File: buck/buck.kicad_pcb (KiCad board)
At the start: 2 copper layers, 37.8 x 17.8 mm, 15 parts, among them IC1 TPS630702RNMR

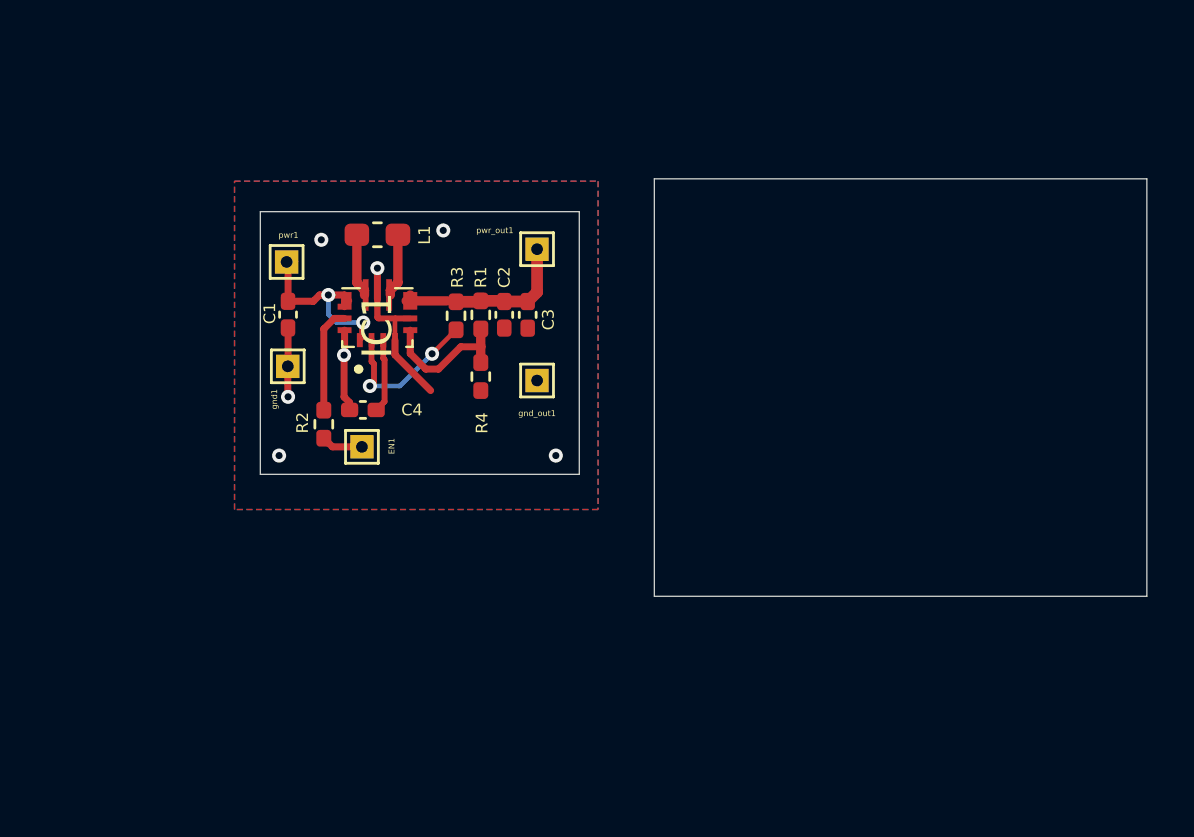
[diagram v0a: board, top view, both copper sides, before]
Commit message: removed esp32 comp
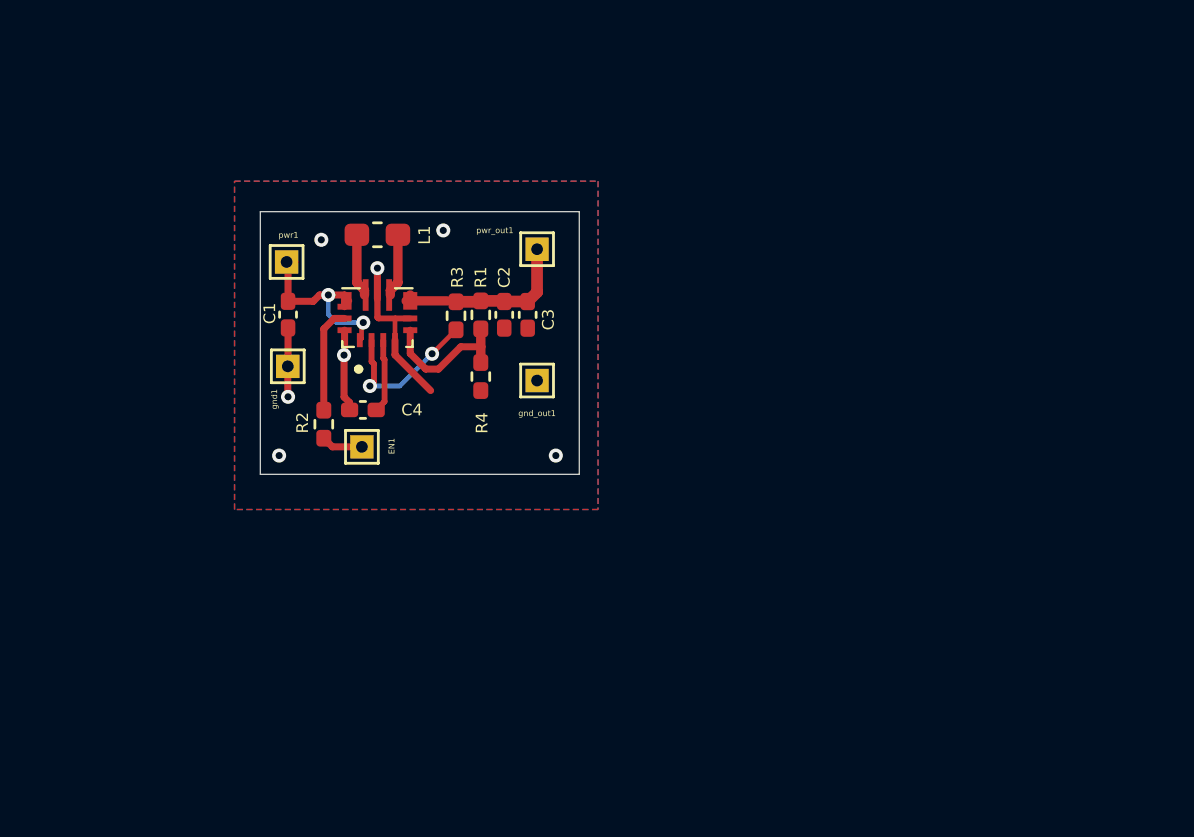
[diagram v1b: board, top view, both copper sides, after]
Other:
- board size 37.8 x 17.8 mm -> 13.6 x 11.2 mm
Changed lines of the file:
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@@
 			(at 0.194 0 90)
 			(layer "F.SilkS")
+			(hide yes)
 			(effects
 				(font
@@
 			)
 			(layer "F.Fab")
-		)
-		(fp_text user "${REFERENCE}"
-			(at 0.194 0 90)
-			(layer "F.Fab")
-			(effects
-				(font
-					(size 1.27 1.27)
-					(thickness 0.254)
-				)
-			)
 		)
 		(pad "1" smd rect
@@
 	)
 	(gr_rect
-		(start 176.4 63.4)
-		(end 197.4 81.2)
-		(stroke
-			(width 0.05)
-			(type default)
-		)
-		(fill no)
-		(layer "Edge.Cuts")
-	)
-	(gr_rect

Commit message: made prod, gave components for everything
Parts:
- C1, C3: footprint Capacitor_SMD:C_0402_1005Metric_Pad0.74x0.62mm_HandSolder -> Capacitor_SMD:C_0805_2012Metric_Pad1.18x1.45mm_HandSolder
- EN: renamed from EN1; footprint TestPoint:TestPoint_THTPad_1.0x1.0mm_Drill0.5mm -> TestPoint:TestPoint_Pad_1.0x1.0mm
- gnd: renamed from gnd1; footprint TestPoint:TestPoint_THTPad_1.0x1.0mm_Drill0.5mm -> TestPoint:TestPoint_Pad_1.0x1.0mm
- gnd_out: renamed from gnd_out1; footprint TestPoint:TestPoint_THTPad_1.0x1.0mm_Drill0.5mm -> TestPoint:TestPoint_Pad_1.0x1.0mm
- pwr_in: renamed from pwr1; footprint TestPoint:TestPoint_THTPad_1.0x1.0mm_Drill0.5mm -> TestPoint:TestPoint_Pad_1.0x1.0mm
- pwr_out: renamed from pwr_out1; footprint TestPoint:TestPoint_THTPad_1.0x1.0mm_Drill0.5mm -> TestPoint:TestPoint_Pad_1.0x1.0mm
- moved gnd 1.10 mm to (160.8, 72.5)
- moved C3 0.53 mm to (171.5, 69.2)
- moved pwr_in 0.40 mm to (160.7, 66.5)
- moved C1 0.33 mm to (160.7, 69.5)
- moved gnd_out 0.22 mm to (171.6, 72.2)
- moved pwr_out 0.18 mm to (171.5, 66.3)
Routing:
- net GND: track 13.8 -> 16.7 mm

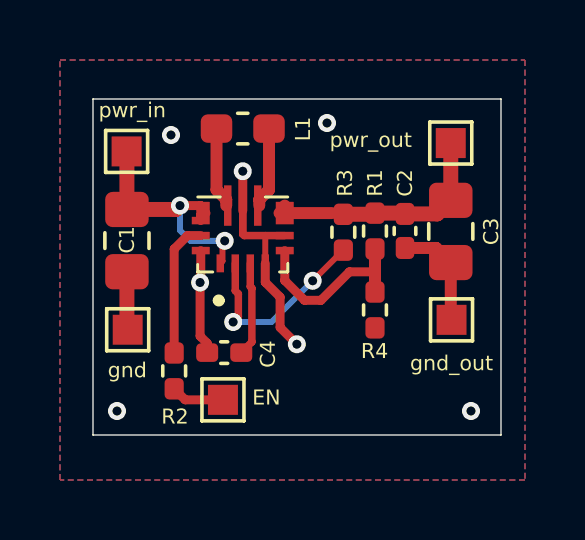
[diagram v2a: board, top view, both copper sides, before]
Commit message: made prod with through hole mounts
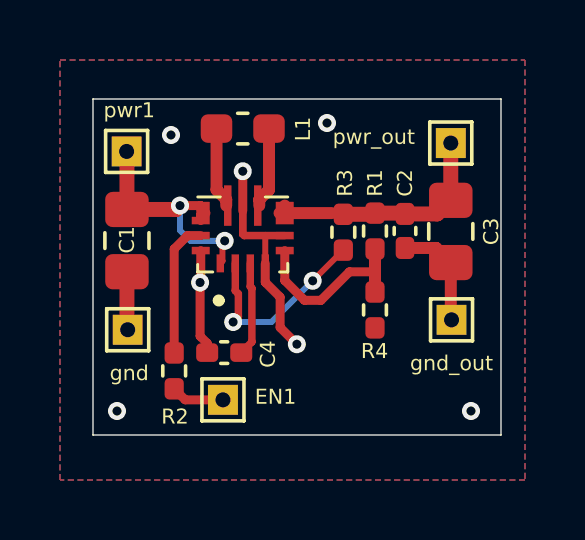
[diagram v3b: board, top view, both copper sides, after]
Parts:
- EN1: renamed from EN; footprint TestPoint:TestPoint_Pad_1.0x1.0mm -> TestPoint:TestPoint_THTPad_1.0x1.0mm_Drill0.5mm
- gnd, gnd_out, pwr_out: footprint TestPoint:TestPoint_Pad_1.0x1.0mm -> TestPoint:TestPoint_THTPad_1.0x1.0mm_Drill0.5mm
- pwr1: renamed from pwr_in; footprint TestPoint:TestPoint_Pad_1.0x1.0mm -> TestPoint:TestPoint_THTPad_1.0x1.0mm_Drill0.5mm
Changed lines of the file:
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@@
 	(net 9 "Net-(IC1-PG)")
 	(net 10 "Net-(EN1-Pad1)")
-	(footprint "TestPoint:TestPoint_Pad_1.0x1.0mm"
+	(footprint "TestPoint:TestPoint_THTPad_1.0x1.0mm_Drill0.5mm"
 		(layer "F.Cu")
 		(at 160.7566 72.4916 90)
-		(descr "SMD rectangular pad as test Point, square 1.0mm side length")
-		(tags "test point SMD pad rectangle square")
+		(descr "THT rectangular pad as test Point, square 1.0mm side length, hole diameter 0.5mm")
+		(tags "test point THT pad rectangle square")
 		(property "Reference" "gnd"
-			(at -1.3512 -0.0142 180)
+			(at -1.4478 0.0508 180)
 			(layer "F.SilkS")
 			(effects
@@
 			(layer "F.CrtYd")
 		)
-		(pad "1" smd rect
+		(pad "1" thru_hole rect
 			(at 0 0 90)
 			(size 1 1)
-			(layers "F.Cu" "F.Mask")
+			(drill 0.5)
+			(layers "*.Cu" "*.Mask")
+			(remove_unused_layers no)
 			(net 2 "GND")
 			(pinfunction "1")
@@
 		)
 	)
-	(footprint "TestPoint:TestPoint_Pad_1.0x1.0mm"
+	(footprint "TestPoint:TestPoint_THTPad_1.0x1.0mm_Drill0.5mm"
 		(layer "F.Cu")
 		(at 160.7208 66.548 90)
-		(descr "SMD rectangular pad as test Point, square 1.0mm side length")
-		(tags "test point SMD pad rectangle square")
-		(property "Reference" "pwr_in"
-			(at 1.3716 0.1882 180)
+		(descr "THT rectangular pad as test Point, square 1.0mm side length, hole diameter 0.5mm")
+		(tags "test point THT pad rectangle square")
+		(property "Reference" "pwr1"
+			(at 1.3716 0.0866 180)
 			(layer "F.SilkS")
 			(effects
@@
 			(layer "F.CrtYd")
 		)
-		(pad "1" smd rect
+		(pad "1" thru_hole rect
 			(at 0 0 90)
 			(size 1 1)
-			(layers "F.Cu" "F.Mask")
+			(drill 0.5)
+			(layers "*.Cu" "*.Mask")
+			(remove_unused_layers no)
 			(net 1 "Net-(IC1-PS{slash}SYNC)")
 			(pinfunction "1")
@@
 		)
 	)
-	(footprint "TestPoint:TestPoint_Pad_1.0x1.0mm"
+	(footprint "TestPoint:TestPoint_THTPad_1.0x1.0mm_Drill0.5mm"
 		(layer "F.Cu")
 		(at 163.9316 74.8284)
-		(descr "SMD rectangular pad as test Point, square 1.0mm side length")
-		(tags "test point SMD pad rectangle square")
-		(property "Reference" "EN"
-			(at 1.4478 -0.0762 180)
+		(descr "THT rectangular pad as test Point, square 1.0mm side length, hole diameter 0.5mm")
+		(tags "test point THT pad rectangle square")
+		(property "Reference" "EN1"
+			(at 1.7526 -0.1016 0)
 			(layer "F.SilkS")
 			(effects
@@
 			(layer "F.CrtYd")
 		)
-		(pad "1" smd rect
+		(pad "1" thru_hole rect
 			(at 0 0)
 			(size 1 1)
-			(layers "F.Cu" "F.Mask")
+			(drill 0.5)
+			(layers "*.Cu" "*.Mask")
+			(remove_unused_layers no)
 			(net 10 "Net-(EN1-Pad1)")
 			(pinfunction "1")
@@
 		)
 	)
-	(footprint "TestPoint:TestPoint_Pad_1.0x1.0mm"
+	(footprint "TestPoint:TestPoint_THTPad_1.0x1.0mm_Drill0.5mm"
 		(layer "F.Cu")
 		(at 171.5262 66.2686)
-		(descr "SMD rectangular pad as test Point, square 1.0mm side length")
-		(tags "test point SMD pad rectangle square")
+		(descr "THT rectangular pad as test Point, square 1.0mm side length, hole diameter 0.5mm")
+		(tags "test point THT pad rectangle square")
 		(property "Reference" "pwr_out"
-			(at -2.667 -0.1016 180)
+			(at -2.5654 -0.2032 0)
 			(layer "F.SilkS")
 			(effects
@@
 			(layer "F.CrtYd")
 		)
-		(pad "1" smd rect
+		(pad "1" thru_hole rect
 			(at 0 0)
 			(size 1 1)
-			(layers "F.Cu" "F.Mask")
+			(drill 0.5)
+			(layers "*.Cu" "*.Mask")
+			(remove_unused_layers no)
 			(net 4 "+3.3V")
 			(pinfunction "1")
@@
 		(embedded_fonts no)
 	)
-	(footprint "TestPoint:TestPoint_Pad_1.0x1.0mm"
+	(footprint "TestPoint:TestPoint_THTPad_1.0x1.0mm_Drill0.5mm"
 		(layer "F.Cu")
 		(at 171.5516 72.1614 180)
-		(descr "SMD rectangular pad as test Point, square 1.0mm side length")
-		(tags "test point SMD pad rectangle square")
+		(descr "THT rectangular pad as test Point, square 1.0mm side length, hole diameter 0.5mm")
+		(tags "test point THT pad rectangle square")
 		(property "Reference" "gnd_out"
 			(at 0 -1.448 180)
@@
 			(layer "F.CrtYd")
 		)
-		(pad "1" smd rect
+		(pad "1" thru_hole rect
 			(at 0 0 180)
 			(size 1 1)
-			(layers "F.Cu" "F.Mask")
+			(drill 0.5)
+			(layers "*.Cu" "*.Mask")
+			(remove_unused_layers no)
 			(net 2 "GND")
 			(pinfunction "1")

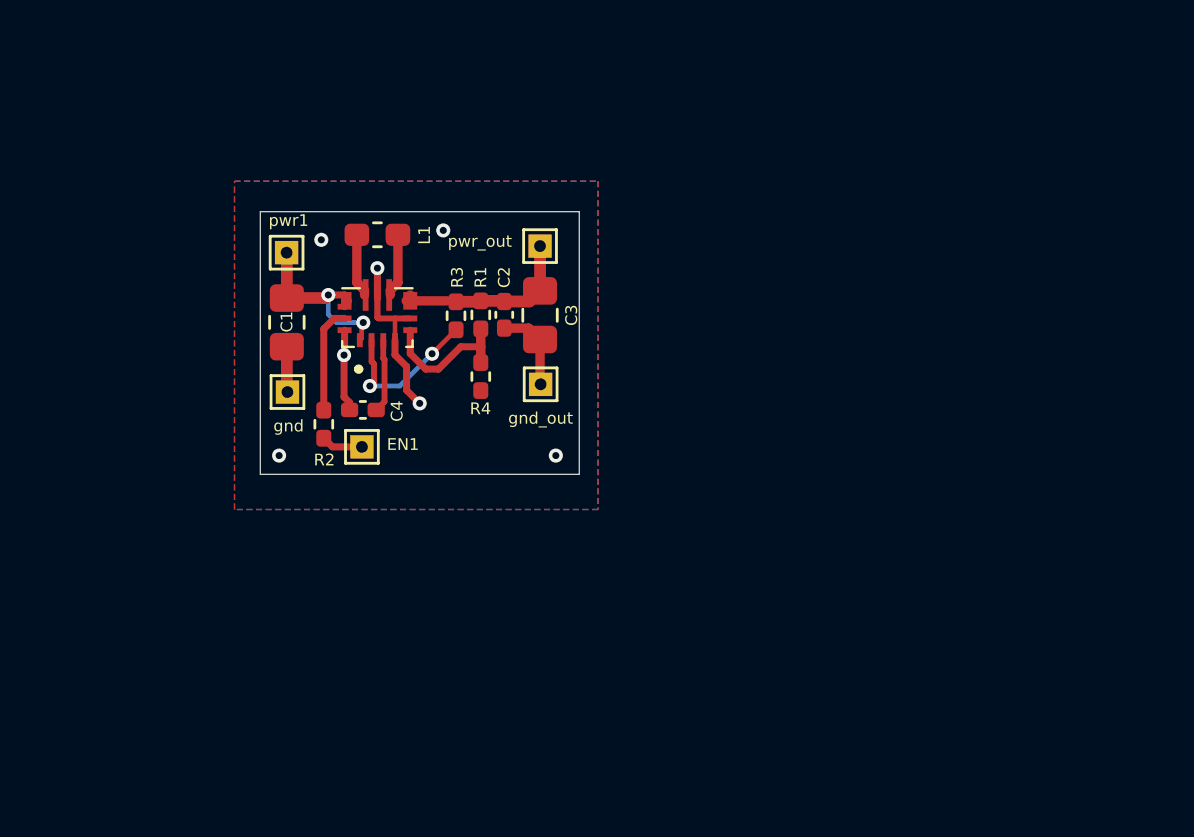
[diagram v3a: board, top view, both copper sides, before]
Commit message: redesigned with new en tie to gnd and 4x pads
added name under IC and near back of board
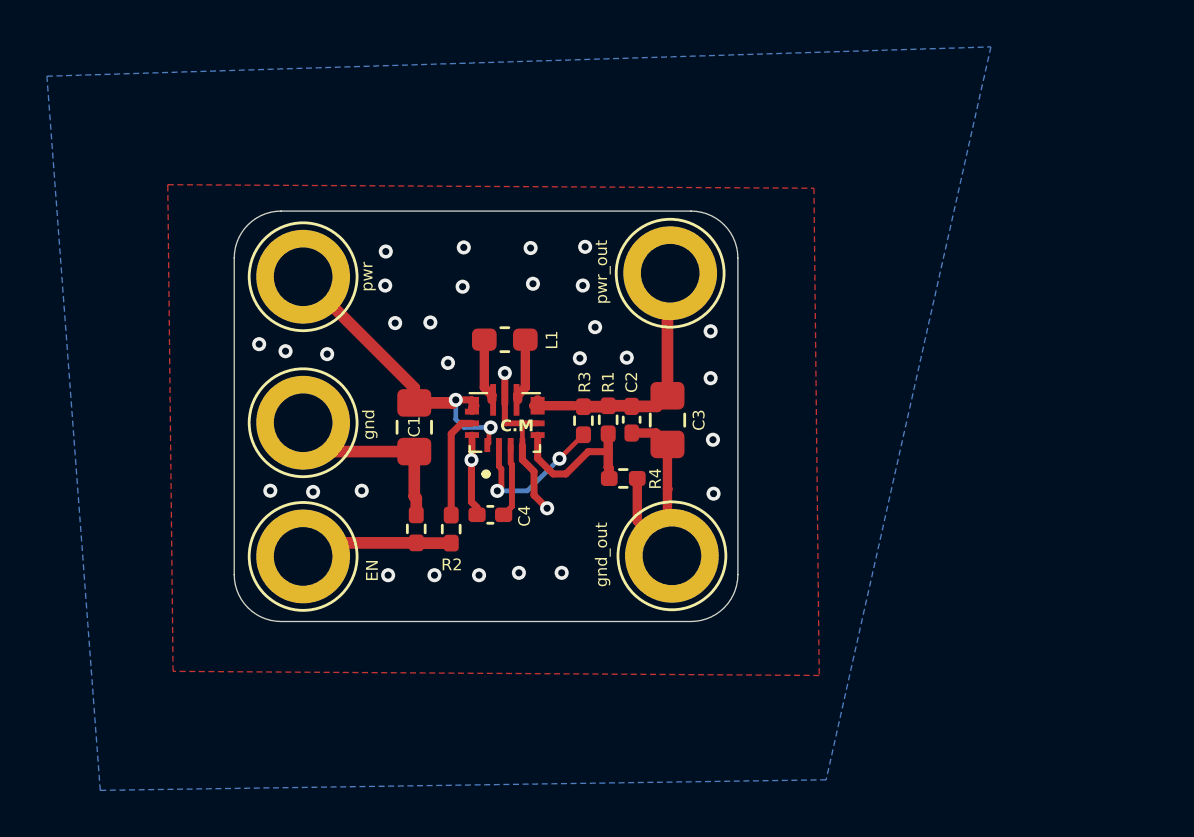
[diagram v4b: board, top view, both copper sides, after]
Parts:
- added R5: 0, Resistor_SMD:R_0402_1005Metric_Pad0.72x0.64mm_HandSolder, F.Cu at (166.2, 78.3)
- EN: renamed from EN1; footprint TestPoint:TestPoint_THTPad_1.0x1.0mm_Drill0.5mm -> TestPoint:TestPoint_Loop_D3.80mm_Drill2.5mm
- gnd, gnd_out, pwr_out: footprint TestPoint:TestPoint_THTPad_1.0x1.0mm_Drill0.5mm -> TestPoint:TestPoint_Loop_D3.80mm_Drill2.5mm
- pwr: renamed from pwr1; footprint TestPoint:TestPoint_THTPad_1.0x1.0mm_Drill0.5mm -> TestPoint:TestPoint_Loop_D3.80mm_Drill2.5mm
- moved gnd_out 9.21 mm to (177.2, 79.5)
- moved R4 7.47 mm to (175.1, 76.2), turned to 180 degrees
- moved C3 7.04 mm to (177.0, 73.7)
- moved R3 7.04 mm to (173.4, 73.7)
- moved C1 7.04 mm to (166.2, 74.0)
- moved C2 7.04 mm to (175.4, 73.7)
- moved C4 7.04 mm to (169.4, 77.7)
- moved IC1 7.04 mm to (170.0, 74.3)
- moved L1 7.04 mm to (170.0, 70.3)
- moved R1 7.04 mm to (174.4, 73.7)
- moved R2 7.04 mm to (167.7, 78.3)
- moved pwr_out 5.67 mm to (177.1, 67.4)
- moved EN 5.30 mm to (161.4, 79.5)
- moved gnd 1.47 mm to (161.4, 73.8), turned to 180 degrees
- moved pwr 1.25 mm to (161.4, 67.6)
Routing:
- net GND: track 16.7 -> 29.6 mm, vias 7 -> 32
- net Net-(IC1-PS/SYNC): track 8.48 -> 13.9 mm
- net Net-(EN1-Pad1): track 1.78 -> 6.62 mm
- net +3.3V: track 7.71 -> 11.1 mm
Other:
- board size 13.6 x 11.2 mm -> 21.5 x 17.5 mm
- board text added: "C.M"
- board text removed: "Made by Caleb Murray"
